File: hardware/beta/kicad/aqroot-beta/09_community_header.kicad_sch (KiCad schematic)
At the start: 37 parts, among them J5 COMMUNITY_HEADER_2x13, U15 TPS22918, U16 TCA9517ADGK

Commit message: AQROOT Beta: lock resolved power and IR component metadata
Records exact MPN / manufacturer / package metadata for four parts whose
selection is now locked. Footprints deliberately left BLANK - locking a part
and verifying its land pattern are separate gates.

  L1   XFL4020-152MEC   Coilcraft                     1.5uH (was '1.5uH XFL4020-152MEC')
  L2   74438357010      Wurth Elektronik              1uH   (was '1uH SHIELDED')
  Q1   AO3400A          Alpha & Omega Semiconductor   AO3400A (was 'NMOS_TBD')
  U16  TCA9517ADGKR     Texas Instruments             TCA9517ADGK (value unchanged)

Instance-level properties only, on stock symbols (Device:L,
Transistor_FET:Q_NMOS_GSD, Logic_LevelTranslator:TCA9517ADGK) - no stock
library was edited and no project-local symbol was touched.

Deliberately NOT recorded, per the no-fabrication rule: Isat, DCR, current
ratings, body dimensions, Vds/Id/Rds(on). Each Note says to take those from
the manufacturer datasheet at BOM lock rather than from memory.

Q1 pin mapping cross-checked against the existing wiring: Q_NMOS_GSD gives
1 Gate / 2 Source / 3 Drain, and the schematic already has 1 -> IR_GATE,
2 -> GND, 3 -> IR_LED_K. Consistent, but the Note flags that AO3400A's real
pin order must be confirmed against the AOS datasheet before a footprint is
assigned. Topology and GPIO mapping unchanged.

L2's Note additionally records that its current rating still has to be
checked against the TI TPS61023 5V design calculation.

U12, U14 and U15 were inspected and already carried complete and correct
metadata - no change was needed. U12's apparent 16-pin/14-pin conflict is
explained by its own Note: pins 15 and 16 are KiCad-only logical numbers for
the unnumbered PGND pad and the exposed thermal pad, so it is a genuine
14-pin DSJ.

Verified with kicad-cli: netlist pin-to-net mapping byte-identical, ERC
unchanged raw 48 / unique 24 / excluded 24 / real 0.

Co-Authored-By: Claude Opus 5 <noreply@anthropic.com>
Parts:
- U16: MPN (none) -> TCA9517ADGKR; Manufacturer (none) -> Texas Instruments; Note (none) -> Community-header I2C buffer. LOCKED 2026-08-07, superseding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; Package (none) -> DGK / VSSOP-8, 3 mm x 3 mm, 0.65 mm pitch - LOCKED. Footpri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
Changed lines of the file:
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@@
+			)
+		)
+		(property "Note" "Community-header I2C buffer. LOCKED 2026-08-07, superseding the earlier TCA9517A / PCA9515A candidate framing. Powered-off high-Z and no accessory-side back-powering still require bring-up validation."
+			(at 229.87 76.2 0)
+			(hide yes)
+			(show_name no)
+			(do_not_autoplace no)
+			(effects
+				(font
+					(size 1.27 1.27)
+				)
+			)
+		)
+		(property "Package" "DGK / VSSOP-8, 3 mm x 3 mm, 0.65 mm pitch - LOCKED. Footprint Package_SO:VSSOP-8_3x3mm_P0.65mm is tagged Texas_DGK0008A but has NOT been compared against the TI DGK land pattern."
+			(at 229.87 76.2 0)
+			(hide yes)
+			(show_name no)
+			(do_not_autoplace no)
+			(effects
+				(font
+					(size 1.27 1.27)
+				)
+			)
+		)
+		(property "Manufacturer" "Texas Instruments"
+			(at 229.87 76.2 0)
+			(hide yes)
+			(show_name no)
+			(do_not_autoplace no)
+			(effects
+				(font
+					(size 1.27 1.27)
+				)
+			)
+		)
+		(property "MPN" "TCA9517ADGKR"
+			(at 229.87 76.2 0)
+			(hide yes)
+			(show_name no)
+			(do_not_autoplace no)
+			(effects
+				(font
+					(size 1.27 1.27)
+				)
 			)
 		)

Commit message: AQROOT Beta: integrate E22 module and dedicate XGPIO14 to RX control
Atomic change across four files - root, sheet 04, sheet 08 and sheet 09 -
because the hierarchy reallocation and the module capture are electrically
coupled and neither is valid alone.

APPLIED TO U8, NOT U7. The schematic is authoritative: U8 is the SX1262 /
E22-900M22S at 915 MHz and U7 remains the CC1101 / E07-400M10S at 433 MHz. The
earlier blocker-register transposition is corrected and annotated in the log;
U7 is untouched and still a placeholder awaiting its own vendor audit.

U8 CAPTURE. The SX1262_MODULE_PLACEHOLDER is replaced by the physical 22-pin
E22-900M22S symbol on AQROOT_Beta:Ebyte_E22-900M22S. All 22 pads resolve, none
unconnected: the ten physical grounds - pins 1 to 5, 10, 11, 12, 20 and 22 - all
land on GND individually rather than being collapsed, pin 9 VCC is on +3V3, and
pins 13 to 19 carry SX1262_DIO1, SX1262_BUSY, SX1262_RST_N, SPI_B_MISO,
SPI_B_MOSI, SPI_B_SCK and SX1262_CS_N respectively. The seven existing
hierarchical labels were relocated onto the new pin stubs rather than
duplicated.

RF SWITCH. DIO2 on pin 8 is strapped locally to TXEN on pin 7, and the netlist
confirms DIO2_TXEN contains exactly those two nodes and nothing else, so no MCU
or expander pin is consumed for transmit control. Firmware must enable
SetDIO2AsRfSwitchCtrl or TXEN never asserts. Receive control comes from
SX1262_RXEN, which contains exactly U3 pin 19, U8 pin 6 and the new R74
pulldown.

XGPIO14 RETIRED. U3 pin 19 is reallocated from XGPIO14 to SX1262_RXEN across the
whole hierarchy - the sheet 08 hierarchical label, the sheet 08 sheet pin in the
root, and a new sheet 04 sheet pin plus root label. On sheet 09 the community
path is removed: R65 and its wires are deleted, the XGPIO14 hierarchical label
is gone, and both XGPIO14_HDR labels become RESERVED_NC, so J5 pin 19 no longer
advertises a GPIO. D6's now-spare ESD channel carries an explicit no_connect.
XGPIO0 to XGPIO13 are untouched and a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
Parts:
- removed R65: 100R 1%, Resistor_SMD:R_0603_1608Metric, symbol Device:R
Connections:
- net XGPIO14_HDR: no longer names the net of D6.4 (IO3)
- net XGPIO14_HDR: no longer J5.19 (Pin_19)
- new net RESERVED_NC: J5.19 (Pin_19)
- no-connect marks 1 -> 2
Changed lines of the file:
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@@
 	)
 	(no_connect
+		(at 153.67 147.32)
+	)
+	(no_connect
 		(at 153.67 152.4)
 	)
@@
 	(wire
 		(pts
-			(xy 156.21 144.78) (xy 156.21 147.32)
-		)
-		(stroke
-			(width 0)
-			(type default)
-		)
-	)
-	(wire
-		(pts
 			(xy 229.87 88.9) (xy 229.87 90.17)
 		)
@@
 	(wire
 		(pts
-			(xy 153.67 147.32) (xy 156.21 147.32)
-		)
-		(stroke
-			(width 0)
-			(type default)
-		)
-	)
-	(wire
-		(pts
 			(xy 213.36 97.79) (xy 215.9 97.79)
 		)
@@
 	(wire
 		(pts
-			(xy 166.37 147.32) (xy 167.64 147.32)
-		)
-		(stroke
-			(width 0)
-			(type default)
-		)
-	)
-	(wire
-		(pts
 			(xy 157.48 114.3) (xy 160.02 114.3)
 		)
@@
 	(wire
 		(pts
-			(xy 156.21 147.32) (xy 158.75 147.32)
-		)
-		(stroke
-			(width 0)
-			(type default)
-		)
-	)
-	(wire
-		(pts
 			(xy 180.34 125.73) (xy 180.34 127)
 		)
@@
 		)
 	)
-	(label "XGPIO14_HDR"
+	(label "RESERVED_NC"
 		(at 251.46 132.08 180)
 		(effects
@@
 		)
 	)
-	(label "XGPIO14_HDR"
+	(label "RESERVED_NC"
 		(at 156.21 144.78 90)
 		(effects
@@
 		)
 	)
-	(hierarchical_label "XGPIO14"
-		(shape bidirectional)
-		(at 167.64 147.32 0)
-		(effects
-			(font
-				(size 1.27 1.27)
-			)
-			(justify left)
-		)
-	)
 	(hierarchical_label "FAST_IO_U0TXD_ROOTPROBE_CS"
 		(shape input)
@@
 					(unit 1)
 				)
-			)
-		)
-	)
-	(symbol
-		(lib_id "Device:R")
-		(at 162.56 147.32 90)
-		(unit 1)
-		(body_style 1)
-		(exclude_from_sim no)
-		(in_bom yes)
-		(on_board yes)
-		(in_pos_files yes)
-		(dnp no)
-		(property "Reference" "R65"
-			(at 162.814 142.494 90)
-			(show_name no)
-			(do_not_autoplace no)
-			(effects
-				(font
-					(size 1.27 1.27)
-				)
-			)
-		)
-		(property "Value" "100R 1%"
-			(at 162.56 144.526 90)
-			(show_name no)
-			(do_not_autoplace no)
-			(effects
-				(font
-					(size 1.27 1.27)
-				)
-			)
-		)
-		(property "Footprint" "Resistor_SMD:R_0603_1608Metric"
-			(at 162.56 149.098 90)
-			(hide yes)
-			(show_name no)
-			(do_not_autoplace no)
-			(effects
-				(font
-					(size 1.27 1.27)
-				)
-			)
-		)
-		(property "Datasheet" ""
-			(at 162.56 147.32 0)
-			(hide yes)
-			(show_name no)
-			(do_not_autoplace no)
-			(effects
-				(font
-					(size 1.27 1.27)
-				)
-			)
-		)
-		(property "Description" "Resistor"
-			(at 162.56 147.32 0)
-			(hide yes)
-			(show_name no)
-			(do_not_autoplace no)
-			(effects
-				(font
-					(size 1.27 1.27)
-				)
-			)
-		)
-		(pin "2"
-		)
-		(pin "1"
-		)
-		(instances
-			(project "aqroot-Beta"
-				(path "/8a0ad1ee-a49e-4cff-9a78-44823e373405/fc294db1-6eef-4bd8-b4f0-c1bd635657ed"
-					(reference "R65")
-					(unit 1)
-				)

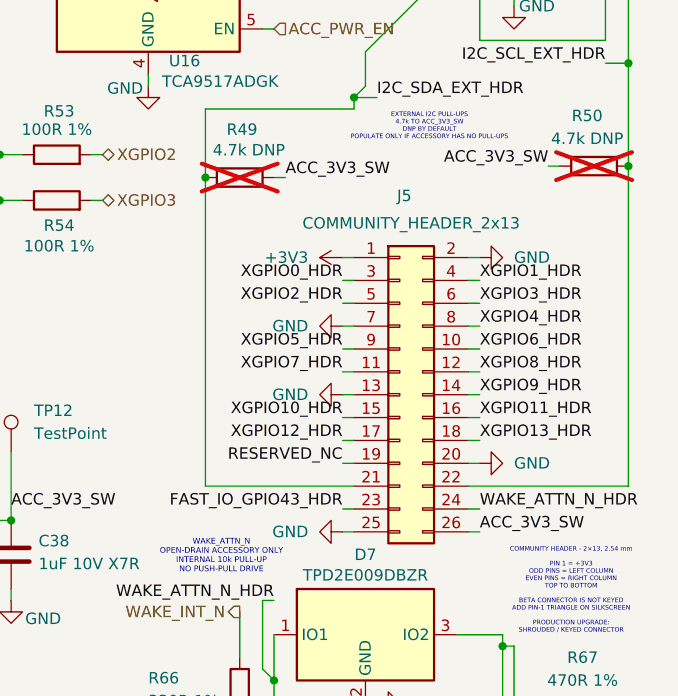
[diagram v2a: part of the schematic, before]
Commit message: Implement F4 J5 pin map and the 19/19 header escape
Land the CTO-approved F4 pin map and the first complete J5 escape. Eight J5
pads move, in exactly three logical swaps -- WAKE <-> GND, the external I2C
pair <-> XGPIO10/11, and ACC <-> RESERVED_NC. No header function is added or
removed: all 14 XGPIO, FAST_IO, external I2C, switched accessory power,
WAKE/ATTN, +3V3 and five grounds are preserved.

Schematic: J5.15/16 take the external I2C names by label. J5.21/22 were
WIRE-bound to the I2C front end (D2, R47/R48 series, R49/R50 pull-ups), so
renaming their remote labels would have aliased the whole front end onto
XGPIO10/11. Instead the two dead-end spurs are cut below the pull-up taps at
(236.22,100.33) and (283.21,99.06), and J5.21/22 get their own stub labels.
WAKE's label and GND #PWR0162 are relocated rather than recreated, so no UUID
or reference designator is minted.

Netlist gate: 176 nets before and after, none added or removed, exactly eight
nets changed, each moving exactly one J5 pad, zero non-J5 node movement.
ERC 116 violations / 10 errors, identical to baseline in every category.

PCB: 207 segments and 24 vias added (271.46 mm of J5 route), GND thermal
relief migrated J5.13 -> J5.24 leaving the override set {2,7,20,24,25}, and
all zones refilled. DRC 241 warnings / 0 errors -- warning parity with
baseline, and refill clears the stale In1-pour artefacts entirely. Header
ratsnest edges 46 -> 27, exactly one removed per routed net; the remainder is
the pre-existing, unrelated ESD-diode sub-network. Every route lands exactly
on a pad of its own net. No footprint moved, no pre-existing copper lost,
Edge.Cuts unchanged, no Option-B / F.Cu / In2 header exception introduced.

Budgets: all 19 pass under the general doctrine. Both pin-specific allowances
are retired rather than transferred -- they existed only because ACC (J5.26,
c1) and WAKE (J5.24, c2) sat above the U3 wall. ACC now measures 7.53 mm
against the ordinary 8.0 mm north-row budget at J5.19, marg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
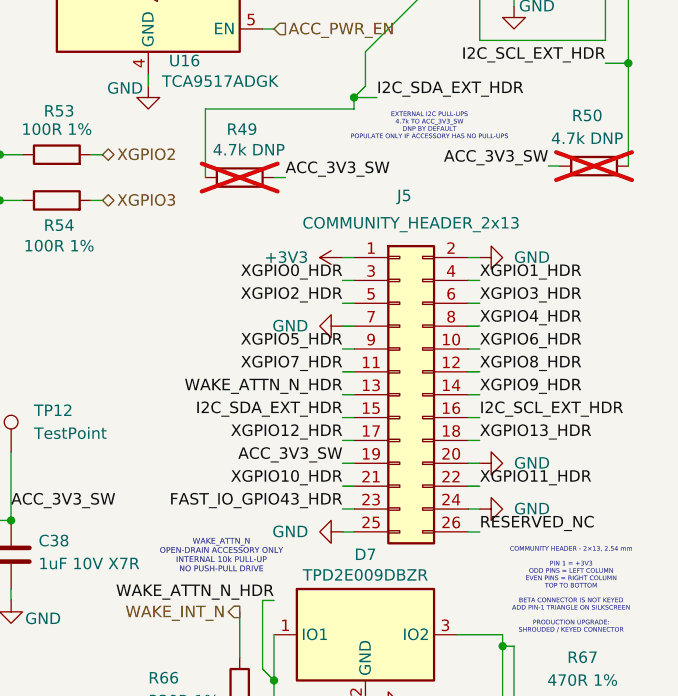
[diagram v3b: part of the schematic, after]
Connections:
- net ACC_3V3_SW: now also J5.19 (Pin_19); no longer J5.26 (Pin_26)
- net GND: now also J5.24 (Pin_24); no longer J5.13 (Pin_13)
- net I2C_SCL_EXT_HDR: now also J5.16 (Pin_16); no longer J5.22 (Pin_22)
- net I2C_SDA_EXT_HDR: now also J5.15 (Pin_15); no longer J5.21 (Pin_21)
- net RESERVED_NC: now also J5.26 (Pin_26); no longer J5.19 (Pin_19)
- net WAKE_ATTN_N_HDR: now also J5.13 (Pin_13); no longer J5.24 (Pin_24)
- net XGPIO10_HDR: now also J5.21 (Pin_21); no longer J5.15 (Pin_15)
- net XGPIO11_HDR: now also J5.22 (Pin_22); no longer J5.16 (Pin_16)
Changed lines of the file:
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@@
 	)
 	(junction
-		(at 236.22 100.33)
-		(diameter 0)
-		(color 0 0 0 0)
-	)
-	(junction
 		(at 180.34 73.66)
 		(diameter 0)
@@
 	)
 	(junction
-		(at 283.21 99.06)
-		(diameter 0)
-		(color 0 0 0 0)
-	)
-	(junction
 		(at 213.36 102.87)
 		(diameter 0)
@@
 	(wire
 		(pts
+			(xy 251.46 134.62) (xy 252.73 134.62)
+		)
+		(stroke
+			(width 0)
+			(type default)
+		)
+	)
+	(wire
+		(pts
+			(xy 265.43 134.62) (xy 266.7 134.62)
+		)
+		(stroke
+			(width 0)
+			(type default)
+		)
+	)
+	(wire
+		(pts
 			(xy 20.32 185.42) (xy 20.32 190.5)
 		)
@@
 	(wire
 		(pts
-			(xy 265.43 134.62) (xy 283.21 134.62)
-		)
-		(stroke
-			(width 0)
-			(type default)
-		)
-	)
-	(wire
-		(pts
 			(xy 259.08 68.58) (xy 252.73 68.58)
 		)
@@
 	(wire
 		(pts
-			(xy 236.22 134.62) (xy 252.73 134.62)
-		)
-		(stroke
-			(width 0)
-			(type default)
-		)
-	)
-	(wire
-		(pts
 			(xy 180.34 124.46) (xy 180.34 125.73)
 		)
@@
 	(wire
 		(pts
-			(xy 236.22 100.33) (xy 236.22 134.62)
-		)
-		(stroke
-			(width 0)
-			(type default)
-		)
-	)
-	(wire
-		(pts
 			(xy 198.12 153.67) (xy 198.12 154.94)
 		)
@@
 	(wire
 		(pts
-			(xy 283.21 99.06) (xy 283.21 134.62)
-		)
-		(stroke
-			(width 0)
-			(type default)
-		)
-	)
-	(wire
-		(pts
 			(xy 210.82 138.43) (xy 214.63 138.43)
 		)
@@
 		)
 	)
+	(label "XGPIO10_HDR"
+		(at 251.46 134.62 180)
+		(effects
+			(font
+				(size 1.27 1.27)
+			)
+			(justify right bottom)
+		)
+	)
+	(label "XGPIO11_HDR"
+		(at 266.7 134.62 0)
+		(effects
+			(font
+				(size 1.27 1.27)
+			)
+			(justify left bottom)
+		)
+	)
 	(label "ACC_3V3_SW"
 		(at 20.32 190.5 0)
@@
 		)
 	)
-	(label "ACC_3V3_SW"
+	(label "RESERVED_NC"
 		(at 266.7 139.7 0)
 		(effects
@@
 		)
 	)
-	(label "RESERVED_NC"
+	(label "ACC_3V3_SW"
 		(at 251.46 132.08 180)
 		(effects
@@
 	)
 	(label "WAKE_ATTN_N_HDR"
-		(at 266.7 137.16 0)
+		(at 251.46 124.46 180)
 		(effects
 			(font
 				(size 1.27 1.27)
 			)
-			(justify left bottom)
+			(justify right bottom)
 		)
 	)
@@
 		)
 	)
-	(label "XGPIO11_HDR"
+	(label "I2C_SCL_EXT_HDR"
 		(at 266.7 127 0)
 		(effects
@@
 		)
 	)
-	(label "XGPIO10_HDR"
+	(label "I2C_SDA_EXT_HDR"
 		(at 251.46 127 180)
 		(effects
@@
 	(symbol
 		(lib_id "power:GND")
-		(at 251.46 124.46 270)
+		(at 266.7 137.16 90)
 		(unit 1)
 		(body_style 1)
@@
 		(fields_autoplaced yes)
 		(property "Reference" "#PWR0162"
-			(at 245.11 124.46 0)
+			(at 273.05 137.16 0)
 			(hide yes)
 			(show_name no)
@@
 		)
 		(property "Value" "GND"
-			(at 247.65 124.4599 90)
+			(at 270.51 137.1599 90)
 			(show_name no)
 			(do_not_autoplace no)
@@
 		)
 		(property "Footprint" ""
-			(at 251.46 124.46 0)
+			(at 266.7 137.16 0)
 			(hide yes)
 			(show_name no)
@@
 		)
 		(property "Datasheet" ""
-			(at 251.46 124.46 0)
+			(at 266.7 137.16 0)
 			(hide yes)
 			(show_name no)
@@
 		)
 		(property "Description" "Power symbol creates a global label with name \"GND\" , ground"
-			(at 251.46 124.46 0)
+			(at 266.7 137.16 0)
 			(hide yes)
 			(show_name no)
